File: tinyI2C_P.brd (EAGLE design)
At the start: 80.8 x 80 mm, 224 parts, among them IC1 74ABT125BQ, IC10 74ABT125BQ, IC11 TPS76318, IC12 74ABT125BQ, IC13 TPS76318, IC14 74ABT125BQ, IC15 TPS76318, IC16 74ABT125BQ, IC2 TPS76318, IC3 TPS76318, IC4 74ABT125BQ, IC5 TPS76318, IC6 74ABT125BQ, IC7 TPS76318, IC8 74ABT125BQ, IC9 TPS76318, U1 LPC824M201JHI33, U2 LPC824M201JHI33, U3 LPC824M201JHI33, U4 LPC824M201JHI33, U5 LPC824M201JHI33, U6 LPC824M201JHI33, U7 LPC824M201JHI33, U8 LPC824M201JHI33, X1 TSW-112-02-S-S, X10 TSW-112-02-S-S, X11 TSW-112-02-S-S, X12 TSW-102-02-S-S, X13 TSW-106-02-S-S-RA, X14 TSW-112-02-S-S, X15 TSW-112-02-S-S, X16 TSW-102-02-S-S, X17 TSW-106-02-S-S-RA, X18 TSW-112-02-S-S, X19 TSW-112-02-S-S, X2 TSW-106-02-S-S-RA, X20 TSW-102-02-S-S, X21 TSW-106-02-S-S-RA, X22 TSW-112-02-S-S, X23 TSW-112-02-S-S, X24 TSW-102-02-S-S, X25 TSW-106-02-S-S-RA, X26 TSW-112-02-S-S, X27 TSW-112-02-S-S, X28 TSW-102-02-S-S, X29 TSW-106-02-S-S-RA, X3 TSW-112-02-S-S, X30 TSW-112-02-S-S, X31 TSW-112-02-S-S, X32 TSW-102-02-S-S, X4 TSW-102-02-S-S, X5 TSW-106-02-S-S-RA, X6 TSW-112-02-S-S, X7 TSW-112-02-S-S, X8 TSW-102-02-S-S, X9 TSW-106-02-S-S-RA

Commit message: [ GERBER ] update
panelized
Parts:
- added TP41, TP42: TPTP07R, testpad:TP07R
- TP4, TP5: value TPTP07R -> TPTP10R; device testpad:TP07R -> testpad:TP10R
- moved TP21 72.0 mm to (70.3, 27.2)
- moved TP22 68.2 mm to (69.6, 30.4)
- moved TP5 51.2 mm to (73.2, 5.00)
- moved TP4 46.2 mm to (15.0, 78.2)
- moved TP26 22.6 mm to (7.30, 58.4)
- moved TP27 22.1 mm to (6.60, 61.6)
- moved TP11 22.0 mm to (28.3, 27.2)
- moved TP31 21.8 mm to (28.3, 58.4)
- moved TP32 21.3 mm to (27.6, 61.6)
- moved TP12 21.3 mm to (27.6, 30.4)
- moved TP16 21.3 mm to (49.3, 27.2)
- moved TP36 21.0 mm to (49.3, 58.4)
- moved TP37 20.5 mm to (48.6, 61.6)
- moved TP17 20.5 mm to (48.6, 30.4)
- moved TP38 10.6 mm to (71.8, 66.6)
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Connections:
- net 1.8V1: now also TP7.TP; no longer TP5.TP
- net 1.8V2: now also TP14.TP; no longer TP12.TP
- net 1.8V3: now also TP19.TP; no longer TP17.TP
- net 1.8V4: now also TP24.TP; no longer TP22.TP
- net 1.8V5: now also TP29.TP; no longer TP27.TP
- net 1.8V6: now also TP34.TP; no longer TP32.TP
- net 1.8V7: now also TP39.TP; no longer TP37.TP
- net 5V1: now also TP6.TP; no longer TP4.TP
- net 5V2: now also TP13.TP; no longer TP11.TP
- net 5V3: now also TP18.TP; no longer TP16.TP
- net 5V4: now also TP23.TP; no longer TP21.TP
- net 5V5: now also TP28.TP; no longer TP26.TP
- net 5V6: now also TP33.TP; no longer TP31.TP
- net 5V7: now also TP38.TP; no longer TP36.TP
- net GND1: now also TP12.TP; no longer TP10.TP
- net GND2: now also TP17.TP; no longer TP15.TP
- net GND3: now also TP22.TP; no longer TP20.TP
- net GND4: now also TP27.TP; no longer TP25.TP
- net GND5: now also TP32.TP; no longer TP30.TP
- net GND6: now also TP37.TP; no longer TP35.TP
- net GND7: now also TP42.TP; no longer TP40.TP
- net SWCLK1: now also TP10.TP; no longer TP6.TP
- net SWCLK2: now also TP15.TP; no longer TP13.TP
- net SWCLK3: now also TP20.TP; no longer TP18.TP
- net SWCLK4: now also TP25.TP; no longer TP23.TP
- net SWCLK5: now also TP30.TP; no longer TP28.TP
- net SWCLK6: now also TP35.TP; no longer TP33.TP
- net SWCLK7: now also TP40.TP; no longer TP38.TP
- net SWDIO1: now also TP11.TP; no longer TP7.TP
- net SWDIO2: now also TP16.TP; no longer TP14.TP
- net SWDIO3: now also TP21.TP; no longer TP19.TP
- net SWDIO4: now also TP26.TP; no longer TP24.TP
- net SWDIO5: now also TP31.TP; no longer TP29.TP
- net SWDIO6: now also TP36.TP; no longer TP34.TP
- net SWDIO7: now also TP41.TP; no longer TP39.TP
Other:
- board size 80.8 x 80 mm -> 83.2 x 83.2 mm

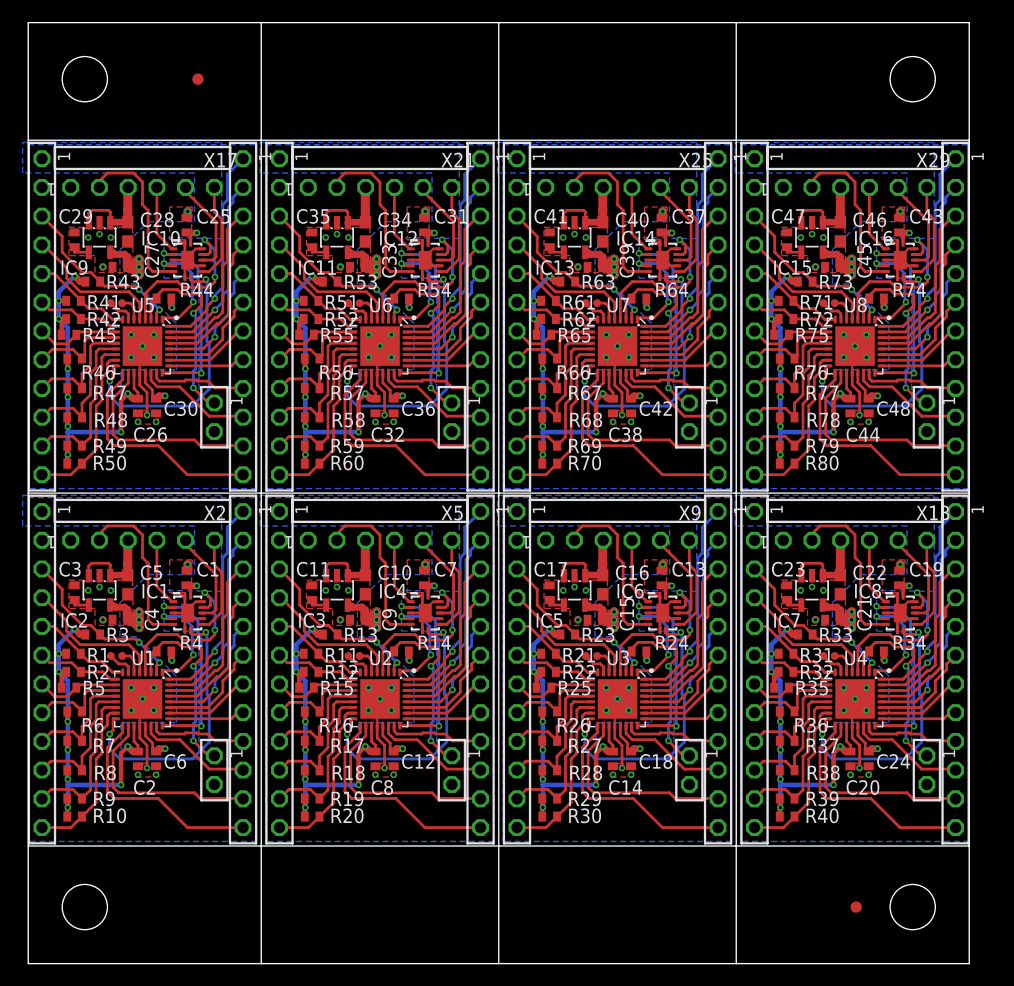
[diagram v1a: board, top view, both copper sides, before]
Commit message: panelized as changed
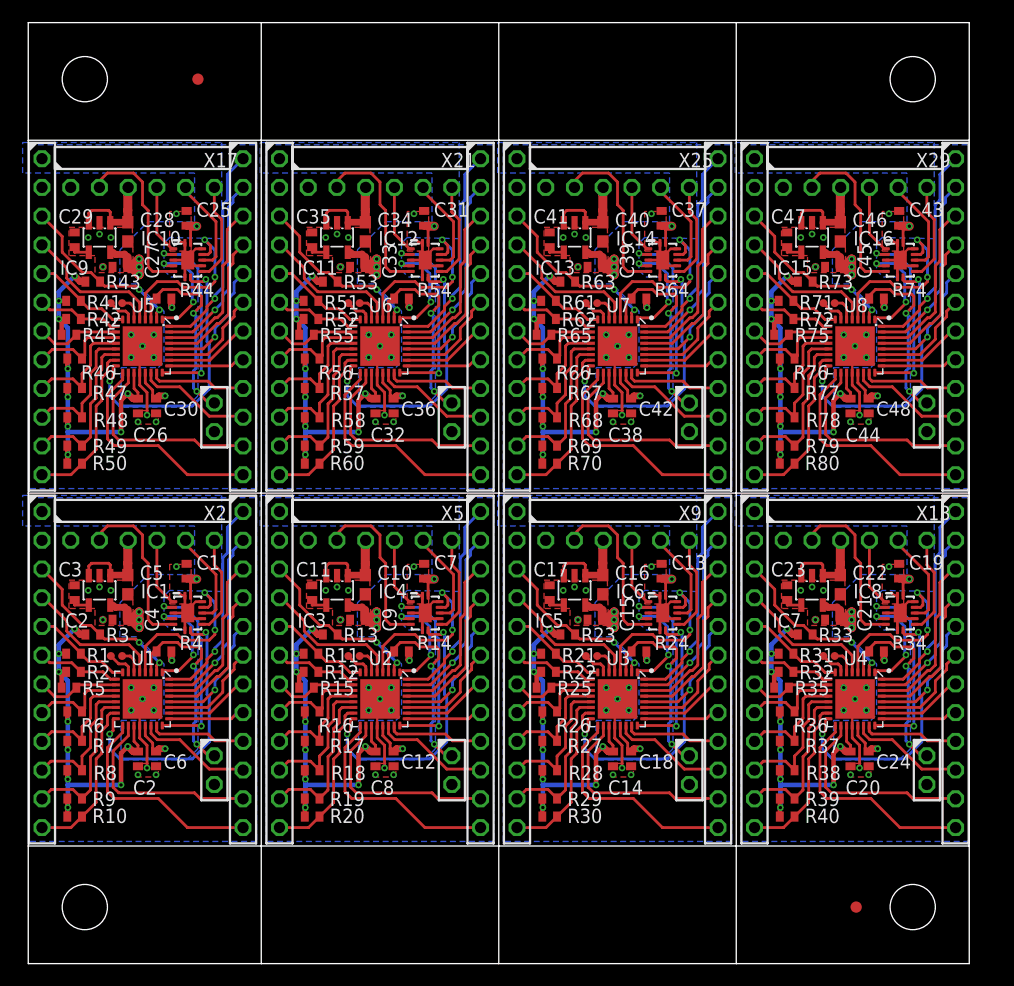
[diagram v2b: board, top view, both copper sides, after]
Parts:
- moved C25 0.60 mm to (14.0, 65.9)
- moved C31 0.60 mm to (35.0, 65.9)
- moved C37 0.60 mm to (56.0, 65.9)
- moved C43 0.60 mm to (77.0, 65.9)
- moved C1 0.60 mm to (14.0, 34.7)
- moved C13 0.60 mm to (56.0, 34.7)
- moved C19 0.60 mm to (77.0, 34.7)
- moved C7 0.60 mm to (35.0, 34.7)
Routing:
- net 1.8V7: track 49.4 -> 50.1 mm
- net 1.8V5: track 49.4 -> 50.1 mm
- net 1.8V4: track 49.4 -> 50.1 mm
- net 1.8V3: track 49.4 -> 50.1 mm
- net 1.8V6: track 49.4 -> 50.1 mm
- net 1.8V2: track 49.4 -> 50.1 mm
- net 1.8V1: track 49.4 -> 50.1 mm
- net 1.8V: track 49.4 -> 50.1 mm
- net GND6: track 15.6 -> 15.0 mm
- net GND5: track 15.6 -> 15.0 mm
- net GND4: track 15.6 -> 15.0 mm
- net GND2: track 15.6 -> 15.0 mm
- net GND1: track 15.6 -> 15.0 mm
- net GND7: track 15.6 -> 15.0 mm
- net GND: track 15.6 -> 15.0 mm
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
